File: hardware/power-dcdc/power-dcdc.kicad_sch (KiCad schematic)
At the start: 69 parts, among them J1 SOLAR_IN, J2 DCDC-MEASURES, J3 DCDC-PWM, J4 BATT2, J5 BATT1, Q1 SIR164ADP, Q2 SIR164ADP, Q3 SI7149ADP, Q4 SI7149ADP, Q5 SI7149ADP, Q6 SI7149ADP, U1 LP4951C, U2 NCP5901B, U3 PAC1953-1, U4 DGD0215, U5 DGD0215

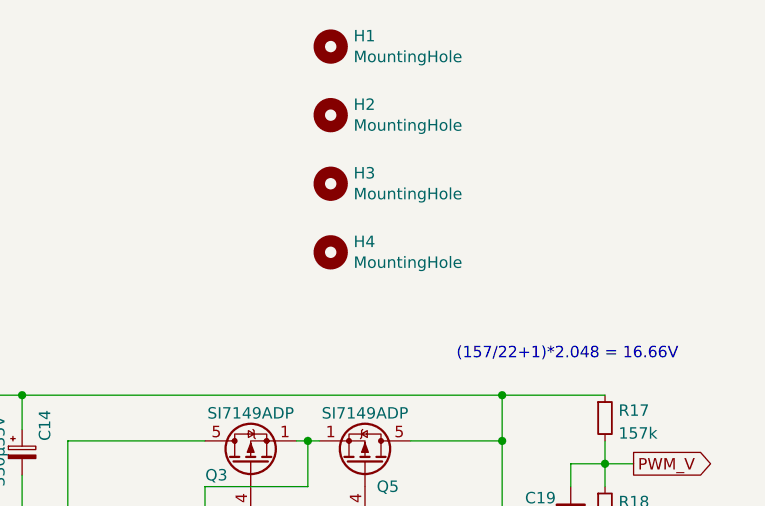
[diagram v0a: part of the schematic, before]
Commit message: Connect mounting holes to GND
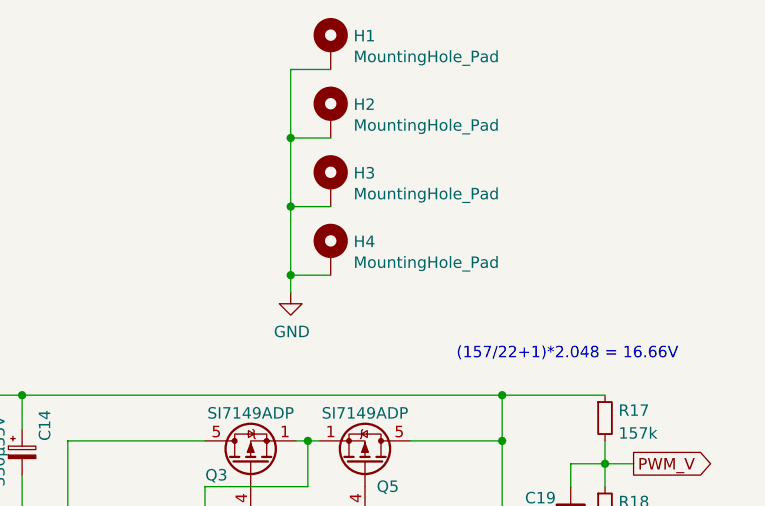
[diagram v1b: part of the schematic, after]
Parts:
- H1, H2, H3, H4: value MountingHole -> MountingHole_Pad; footprint MountingHole:MountingHole_3.2mm_M3_DIN965 -> MountingHole:MountingHole_3.2mm_M3_DIN965_Pad; symbol Mechanical:MountingHole -> Mechanical:MountingHole_Pad
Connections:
- net GND: now also H1.1, H2.1, H3.1, H4.1
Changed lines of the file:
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@@
   (junction (at 59.69 139.7) (diameter 0) (color 0 0 0 0)
   )
+  (junction (at 234.315 29.845) (diameter 0) (color 0 0 0 0)
+  )
   (junction (at 96.52 29.21) (diameter 0) (color 0 0 0 0)
   )
@@
   )
   (junction (at 114.3 73.66) (diameter 0) (color 0 0 0 0)
+  )
+  (junction (at 234.315 45.085) (diameter 0) (color 0 0 0 0)
+  )
+  (junction (at 234.315 37.465) (diameter 0) (color 0 0 0 0)
   )
   (junction (at 81.28 40.64) (diameter 0) (color 0 0 0 0)
@@
     (stroke (width 0) (type default) (color 0 0 0 0))
   )
+  (wire (pts (xy 234.315 37.465) (xy 234.315 29.845))
+    (stroke (width 0) (type default) (color 0 0 0 0))
+  )
   (wire (pts (xy 157.48 134.62) (xy 191.77 134.62))
     (stroke (width 0) (type default) (color 0 0 0 0))
@@
     (stroke (width 0) (type default) (color 0 0 0 0))
   )
+  (wire (pts (xy 234.315 37.465) (xy 238.76 37.465))
+    (stroke (width 0) (type default) (color 0 0 0 0))
+  )
   (wire (pts (xy 109.855 114.3) (xy 109.855 119.38))
     (stroke (width 0) (type default) (color 0 0 0 0))
@@
     (stroke (width 0) (type default) (color 0 0 0 0))
   )
+  (wire (pts (xy 234.315 29.845) (xy 238.76 29.845))
+    (stroke (width 0) (type default) (color 0 0 0 0))
+  )
   (wire (pts (xy 234.95 97.79) (xy 236.22 97.79))
     (stroke (width 0) (type default) (color 0 0 0 0))
@@
     (stroke (width 0) (type default) (color 0 0 0 0))
   )
+  (wire (pts (xy 234.315 45.085) (xy 238.76 45.085))
+    (stroke (width 0) (type default) (color 0 0 0 0))
+  )
   (wire (pts (xy 104.14 29.21) (xy 104.14 33.02))
     (stroke (width 0) (type default) (color 0 0 0 0))
@@
     (stroke (width 0) (type default) (color 0 0 0 0))
   )
+  (wire (pts (xy 234.315 29.845) (xy 234.315 22.225))
+    (stroke (width 0) (type default) (color 0 0 0 0))
+  )
   (wire (pts (xy 81.28 38.1) (xy 81.28 40.64))
     (stroke (width 0) (type default) (color 0 0 0 0))
@@
     (stroke (width 0) (type default) (color 0 0 0 0))
   )
+  (wire (pts (xy 234.315 46.99) (xy 234.315 45.085))
+    (stroke (width 0) (type default) (color 0 0 0 0))
+  )
   (wire (pts (xy 83.82 139.7) (xy 83.82 119.38))
     (stroke (width 0) (type default) (color 0 0 0 0))
@@
     (stroke (width 0) (type default) (color 0 0 0 0))
   )
+  (wire (pts (xy 234.315 45.085) (xy 234.315 37.465))
+    (stroke (width 0) (type default) (color 0 0 0 0))
+  )
   (wire (pts (xy 105.41 134.62) (xy 105.41 142.24))
     (stroke (width 0) (type default) (color 0 0 0 0))
@@
   )
   (wire (pts (xy 93.98 54.61) (xy 96.52 54.61))
+    (stroke (width 0) (type default) (color 0 0 0 0))
+  )
+  (wire (pts (xy 234.315 22.225) (xy 238.76 22.225))
     (stroke (width 0) (type default) (color 0 0 0 0))
   )
@@
     (pin "2")
   )
-  (symbol (lib_id "Mechanical:MountingHole") (at 238.76 19.685 0) (unit 1)
+  (symbol (lib_id "Mechanical:MountingHole_Pad") (at 238.76 19.685 0) (unit 1)
     (in_bom yes) (on_board yes)
     (property "Reference" "H1" (id 0) (at 241.3 18.5166 0)
       (effects (font (size 1.27 1.27)) (justify left))
     )
-    (property "Value" "MountingHole" (id 1) (at 241.3 20.828 0)
-      (effects (font (size 1.27 1.27)) (justify left))
-    )
-    (property "Footprint" "MountingHole:MountingHole_3.2mm_M3_DIN965" (id 2) (at 238.76 19.685 0)
+    (property "Value" "MountingHole_Pad" (id 1) (at 241.3 20.828 0)
+      (effects (font (size 1.27 1.27)) (justify left))
+    )
+    (property "Footprint" "MountingHole:MountingHole_3.2mm_M3_DIN965_Pad" (id 2) (at 238.76 19.685 0)
       (effects (font (size 1.27 1.27)) hide)
     )
@@
       (effects (font (size 1.27 1.27)) hide)
     )
+    (pin "1")
   )
   (symbol (lib_id "Device:C_Small") (at 132.08 48.26 270) (unit 1)
@@
     (pin "1")
   )
-  (symbol (lib_id "Mechanical:MountingHole") (at 238.76 42.545 0) (unit 1)
+  (symbol (lib_id "Mechanical:MountingHole_Pad") (at 238.76 42.545 0) (unit 1)
     (in_bom yes) (on_board yes)
     (property "Reference" "H4" (id 0) (at 241.3 41.3766 0)
       (effects (font (size 1.27 1.27)) (justify left))
     )
-    (property "Value" "MountingHole" (id 1) (at 241.3 43.688 0)
-      (effects (font (size 1.27 1.27)) (justify left))
-    )
-    (property "Footprint" "MountingHole:MountingHole_3.2mm_M3_DIN965" (id 2) (at 238.76 42.545 0)
+    (property "Value" "MountingHole_Pad" (id 1) (at 241.3 43.688 0)
+      (effects (font (size 1.27 1.27)) (justify left))
+    )
+    (property "Footprint" "MountingHole:MountingHole_3.2mm_M3_DIN965_Pad" (id 2) (at 238.76 42.545 0)
       (effects (font (size 1.27 1.27)) hide)
     )
@@
       (effects (font (size 1.27 1.27)) hide)
     )
+    (pin "1")
   )
   (symbol (lib_id "power:+5V") (at 52.07 46.99 0) (unit 1)
@@
     (pin "2")
   )
-  (symbol (lib_id "Mechanical:MountingHole") (at 238.76 34.925 0) (unit 1)
+  (symbol (lib_id "Mechanical:MountingHole_Pad") (at 238.76 34.925 0) (unit 1)
     (in_bom yes) (on_board yes)
     (property "Reference" "H3" (id 0) (at 241.3 33.7566 0)
       (effects (font (size 1.27 1.27)) (justify left))
     )
-    (property "Value" "MountingHole" (id 1) (at 241.3 36.068 0)
-      (effects (font (size 1.27 1.27)) (justify left))
-    )
-    (property "Footprint" "MountingHole:MountingHole_3.2mm_M3_DIN965" (id 2) (at 238.76 34.925 0)
+    (property "Value" "MountingHole_Pad" (id 1) (at 241.3 36.068 0)
+      (effects (font (size 1.27 1.27)) (justify left))
+    )
+    (property "Footprint" "MountingHole:MountingHole_3.2mm_M3_DIN965_Pad" (id 2) (at 238.76 34.925 0)
       (effects (font (size 1.27 1.27)) hide)
     )
@@
       (effects (font (size 1.27 1.27)) hide)
     )
+    (pin "1")
   )
   (symbol (lib_id "power:GND") (at 234.95 142.24 270) (unit 1)
@@
     (pin "2")
   )
-  (symbol (lib_id "Mechanical:MountingHole") (at 238.76 27.305 0) (unit 1)
+  (symbol (lib_id "Mechanical:MountingHole_Pad") (at 238.76 27.305 0) (unit 1)
     (in_bom yes) (on_board yes)
     (property "Reference" "H2" (id 0) (at 241.3 26.1366 0)
       (effects (font (size 1.27 1.27)) (justify left))
     )
-    (property "Value" "MountingHole" (id 1) (at 241.3 28.448 0)
-      (effects (font (size 1.27 1.27)) (justify left))
-    )
-    (property "Footprint" "MountingHole:MountingHole_3.2mm_M3_DIN965" (id 2) (at 238.76 27.305 0)
+    (property "Value" "MountingHole_Pad" (id 1) (at 241.3 28.448 0)
+      (effects (font (size 1.27 1.27)) (justify left))
+    )
+    (property "Footprint" "MountingHole:MountingHole_3.2mm_M3_DIN965_Pad" (id 2) (at 238.76 27.305 0)
       (effects (font (size 1.27 1.27)) hide)
     )
@@
       (effects (font (size 1.27 1.27)) hide)
     )
+    (pin "1")
   )
   (symbol (lib_id "Device:R_Small") (at 111.76 142.24 270) (unit 1)
@@
     )
     (property "Datasheet" "" (id 3) (at 86.36 90.17 0)
+      (effects (font (size 1.27 1.27)) hide)
+    )
+    (pin "1")
+  )
+  (symbol (lib_id "power:GND") (at 234.315 46.99 0) (unit 1)
+    (in_bom yes) (on_board yes)
+    (property "Reference" "#PWR024" (id 0) (at 234.315 53.34 0)
+      (effects (font (size 1.27 1.27)) hide)
+    )
+    (property "Value" "GND" (id 1) (at 234.442 51.3842 0))
+    (property "Footprint" "" (id 2) (at 234.315 46.99 0)
+      (effects (font (size 1.27 1.27)) hide)
+    )
+    (property "Datasheet" "" (id 3) (at 234.315 46.99 0)
       (effects (font (size 1.27 1.27)) hide)
     )
@@
       (reference "#PWR023") (unit 1) (value "GND") (footprint "")
     )
+    (path "/d0316b86-13cf-41da-ae94-6e550ef1990f"
+      (reference "#PWR024") (unit 1) (value "GND") (footprint "")
+    )
     (path "/e2f6369a-02b5-4d5b-ba47-235a0926e866"
       (reference "C1") (unit 1) (value "YFF31HC") (footprint "local:C_filter_1206")
@@
     )
     (path "/1e487dd6-ed86-421b-b7c0-9a9e02f46e66"
-      (reference "H1") (unit 1) (value "MountingHole") (footprint "MountingHole:MountingHole_3.2mm_M3_DIN965")
+      (reference "H1") (unit 1) (value "MountingHole_Pad") (footprint "MountingHole:MountingHole_3.2mm_M3_DIN965_Pad")
     )
     (path "/b986ae44-aeaa-4fb0-b116-e1d4a0c5aba2"
-      (reference "H2") (unit 1) (value "MountingHole") (footprint "MountingHole:MountingHole_3.2mm_M3_DIN965")
+      (reference "H2") (unit 1) (value "MountingHole_Pad") (footprint "MountingHole:MountingHole_3.2mm_M3_DIN965_Pad")
     )
     (path "/aa969c6f-5d2b-46f2-9d16-00677a06a293"
-      (reference "H3") (unit 1) (value "MountingHole") (footprint "MountingHole:MountingHole_3.2mm_M3_DIN965")
+      (reference "H3") (unit 1) (value "MountingHole_Pad") (footprint "MountingHole:MountingHole_3.2mm_M3_DIN965_Pad")
     )
     (path "/22812a7a-1ebf-4a05-8131-0142c56572c4"
-      (reference "H4") (unit 1) (value "MountingHole") (footprint "MountingHole:MountingHole_3.2mm_M3_DIN965")
+      (reference "H4") (unit 1) (value "MountingHole_Pad") (footprint "MountingHole:MountingHole_3.2mm_M3_DIN965_Pad")
     )
     (path "/aa755b7a-e588-473b-b610-150eeceb2729"

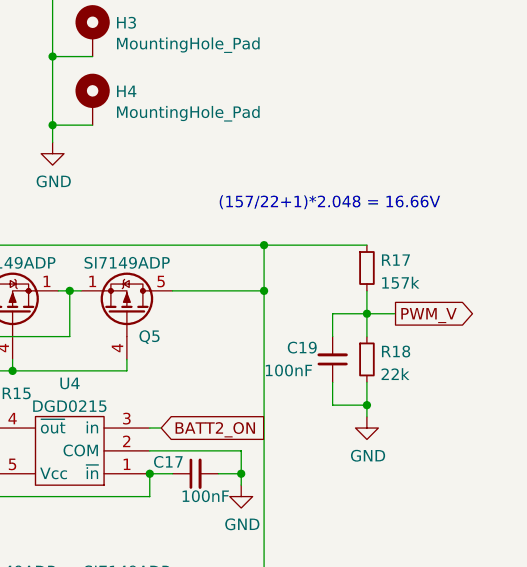
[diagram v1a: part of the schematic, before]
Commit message: Change some resistor values to match available ones.
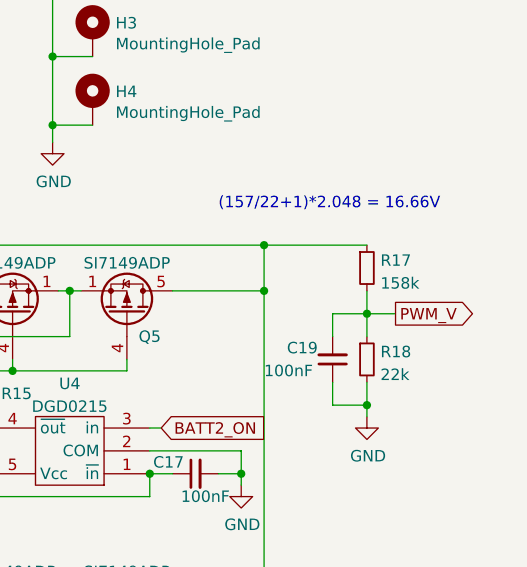
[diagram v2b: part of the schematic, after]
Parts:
- R17: value 157k -> 158k
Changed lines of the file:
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@@
       (effects (font (size 1.27 1.27)) (justify left))
     )
-    (property "Value" "157k" (id 1) (at 270.7386 62.6622 0)
+    (property "Value" "158k" (id 1) (at 270.7386 62.6622 0)
       (effects (font (size 1.27 1.27)) (justify left))
     )
@@
     )
     (path "/b417ac19-37b1-4efe-b1ee-3d38950c8e30"
-      (reference "R17") (unit 1) (value "157k") (footprint "Resistor_SMD:R_0805_2012Metric_Pad1.20x1.40mm_HandSolder")
+      (reference "R17") (unit 1) (value "158k") (footprint "Resistor_SMD:R_0805_2012Metric_Pad1.20x1.40mm_HandSolder")
     )
     (path "/b3d072d8-b65a-4fbe-9091-9d81eb179610"

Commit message: Final pass on part numbers
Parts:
- C1, C15, C16: P/N YFF31HC2A104M -> YFF31HC2A104M (M)
- C11: P/N C1206C104K5RACTU -> C1206C104K5RACTU (M)
- C13, C14, C5, C6: P/N A780MS337M1VLAS020 -> A780MS337M1VLAS020 (F)
- C3, C4: P/N GRM31CR71H475KA12L -> GRM31CR71H475KA12L (M)
- C9: P/N CL31A226KAHNNN -> CL31A226KAHNNN (M)
- D1: P/N (none) -> SMBJ28A (F)
- D2, D3: P/N (none) -> SMBJ16Ae3/TR13 (M)
- H1, H2, H3, H4: P/N (none) -> N/A
- J2, J3: P/N SSW-105-01-T-D -> SSW-105-01-T-D (F)
- L1: P/N 2305-H-RC -> 2305-H-RC (M)
- Q1, Q2: P/N SIR164ADP-T1-GE3 -> SIR164ADP-T1-GE3 (F)
- Q3, Q4, Q5, Q6: P/N SIR164ADP-T1-GE3 -> SI7149ADP-T1-GE3 (M)
- R17: P/N (none) -> CR0805-FX-1583ELF (M)
- R18, R2: P/N (none) -> WF08P2202FTL (F)
- R3: P/N (none) -> stock
- R6: P/N (none) -> WF08P2703FTL (F)
- TH1: P/N NT06104F3950B1H -> NT06104F3950B1H (M)
- U1: P/N LP4951CM/NOPB -> LP4951CM/NOPB (M)
- U2: P/N NCP5901BDR2G -> NCP5901BDR2G (M)
- U4, U5: P/N DGD0215 -> DGD0215WT-7 (M)
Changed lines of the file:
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@@
       (effects (font (size 1.27 1.27)) hide)
     )
-    (property "P/N" "DGD0215" (id 4) (at 236.22 81.28 0)
+    (property "P/N" "DGD0215WT-7 (M)" (id 4) (at 236.22 81.28 0)
       (effects (font (size 1.27 1.27)) hide)
     )
@@
       (effects (font (size 1.27 1.27)) hide)
     )
-    (property "P/N" "A780MS337M1VLAS020" (id 4) (at 204.47 64.77 0)
+    (property "P/N" "A780MS337M1VLAS020 (F)" (id 4) (at 204.47 64.77 0)
       (effects (font (size 1.27 1.27)) hide)
     )
@@
       (effects (font (size 1.27 1.27)) hide)
     )
-    (property "P/N" "A780MS337M1VLAS020" (id 4) (at 104.14 35.56 0)
+    (property "P/N" "A780MS337M1VLAS020 (F)" (id 4) (at 104.14 35.56 0)
       (effects (font (size 1.27 1.27)) hide)
     )
@@
     )
     (property "Datasheet" "https://www.vishay.com/docs/88301/15ke.pdf" (id 3) (at 245.11 148.59 0)
+      (effects (font (size 1.27 1.27)) hide)
+    )
+    (property "P/N" " SMBJ16Ae3/TR13 (M)" (id 4) (at 245.11 147.32 0)
       (effects (font (size 1.27 1.27)) hide)
     )
@@
       (effects (font (size 1.27 1.27)) hide)
     )
-    (property "P/N" "NCP5901BDR2G" (id 4) (at 132.08 59.69 0)
+    (property "P/N" "NCP5901BDR2G (M)" (id 4) (at 132.08 59.69 0)
       (effects (font (size 1.27 1.27)) hide)
     )
@@
       (effects (font (size 1.27 1.27)) hide)
     )
+    (property "P/N" "N/A" (id 4) (at 238.76 19.685 0)
+      (effects (font (size 1.27 1.27)) hide)
+    )
     (pin "1")
   )
@@
       (effects (font (size 1.27 1.27)) hide)
     )
-    (property "P/N" "SIR164ADP-T1-GE3" (id 4) (at 154.94 66.04 0)
+    (property "P/N" "SIR164ADP-T1-GE3 (F)" (id 4) (at 154.94 66.04 0)
       (effects (font (size 1.27 1.27)) hide)
     )
@@
       (effects (font (size 1.27 1.27)) hide)
     )
+    (property "P/N" "N/A" (id 4) (at 238.76 42.545 0)
+      (effects (font (size 1.27 1.27)) hide)
+    )
     (pin "1")
   )
@@
       (effects (font (size 1.27 1.27)) hide)
     )
-    (property "P/N" "SIR164ADP-T1-GE3" (id 4) (at 154.94 50.8 0)
+    (property "P/N" "SIR164ADP-T1-GE3 (F)" (id 4) (at 154.94 50.8 0)
       (effects (font (size 1.27 1.27)) hide)
     )
@@
       (effects (font (size 1.27 1.27)) hide)
     )
+    (property "P/N" "WF08P2202FTL (F)" (id 4) (at 56.515 73.025 0)
+      (effects (font (size 1.27 1.27)) hide)
+    )
     (pin "1")
     (pin "2")
@@
       (effects (font (size 1.27 1.27)) hide)
     )
-    (property "P/N" "A780MS337M1VLAS020" (id 4) (at 96.52 35.56 0)
+    (property "P/N" "A780MS337M1VLAS020 (F)" (id 4) (at 96.52 35.56 0)
       (effects (font (size 1.27 1.27)) hide)
     )
@@
       (effects (font (size 1.27 1.27)) hide)
     )
-    (property "P/N" "A780MS337M1VLAS020" (id 4) (at 196.85 64.77 0)
+    (property "P/N" "A780MS337M1VLAS020 (F)" (id 4) (at 196.85 64.77 0)
       (effects (font (size 1.27 1.27)) hide)
     )
@@
       (effects (font (size 1.27 1.27)) hide)
     )
-    (property "P/N" "YFF31HC2A104M" (id 4) (at 236.22 137.16 0)
+    (property "P/N" "YFF31HC2A104M (M)" (id 4) (at 236.22 137.16 0)
       (effects (font (size 1.27 1.27)) hide)
     )
@@
       (effects (font (size 1.27 1.27)) (justify left) hide)
     )
-    (property "P/N" "SIR164ADP-T1-GE3" (id 4) (at 229.87 66.04 0)
+    (property "P/N" " SI7149ADP-T1-GE3 (M)" (id 4) (at 229.87 66.04 0)
       (effects (font (size 1.27 1.27)) hide)
     )
@@
       (effects (font (size 1.27 1.27)) (justify left) hide)
     )
-    (property "P/N" "SIR164ADP-T1-GE3" (id 4) (at 229.87 100.33 0)
+    (property "P/N" " SI7149ADP-T1-GE3 (M)" (id 4) (at 229.87 100.33 0)
       (effects (font (size 1.27 1.27)) hide)
     )
@@
     )
     (property "Datasheet" "https://www.vishay.com/docs/88301/15ke.pdf" (id 3) (at 245.11 135.89 0)
+      (effects (font (size 1.27 1.27)) hide)
+    )
+    (property "P/N" " SMBJ16Ae3/TR13 (M)" (id 4) (at 245.11 134.62 0)
       (effects (font (size 1.27 1.27)) hide)
     )
@@
       (effects (font (size 1.27 1.27)) hide)
     )
+    (property "P/N" "WF08P2703FTL (F)" (id 4) (at 86.36 49.53 0)
+      (effects (font (size 1.27 1.27)) hide)
+    )
     (pin "1")
     (pin "2")
@@
       (effects (font (size 1.27 1.27)) hide)
     )
-    (property "P/N" " NT06104F3950B1H " (id 4) (at 142.875 89.535 0)
+    (property "P/N" "NT06104F3950B1H (M)" (id 4) (at 142.875 89.535 0)
       (effects (font (size 1.27 1.27)) hide)
     )
@@
       (effects (font (size 1.27 1.27)) hide)
     )
+    (property "P/N" "N/A" (id 4) (at 238.76 34.925 0)
+      (effects (font (size 1.27 1.27)) hide)
+    )
     (pin "1")
   )
@@
       (effects (font (size 1.27 1.27)) hide)
     )
-    (property "P/N" "GRM31CR71H475KA12L" (id 4) (at 88.9 35.56 0)
+    (property "P/N" "GRM31CR71H475KA12L (M)" (id 4) (at 88.9 35.56 0)
       (effects (font (size 1.27 1.27)) hide)
     )
@@
       (effects (font (size 1.27 1.27)) hide)
     )
+    (property "P/N" "WF08P2202FTL (F)" (id 4) (at 269.24 71.12 0)
+      (effects (font (size 1.27 1.27)) hide)
+    )
     (pin "1")
     (pin "2")
@@
     )
     (property "Datasheet" "~" (id 3) (at 269.24 60.96 0)
+      (effects (font (size 1.27 1.27)) hide)
+    )
+    (property "P/N" "CR0805-FX-1583ELF (M)" (id 4) (at 269.24 60.96 0)
       (effects (font (size 1.27 1.27)) hide)
     )
@@
       (effects (font (size 1.27 1.27)) (justify left) hide)
     )
-    (property "P/N" "SIR164ADP-T1-GE3" (id 4) (at 242.57 100.33 0)
+    (property "P/N" " SI7149ADP-T1-GE3 (M)" (id 4) (at 242.57 100.33 0)
       (effects (font (size 1.27 1.27)) hide)
     )
@@
       (effects (font (size 1.27 1.27)) hide)
     )
+    (property "P/N" " SMBJ28A (F)" (id 4) (at 59.69 146.05 0)
+      (effects (font (size 1.27 1.27)) hide)
+    )
     (pin "1")
     (pin "2")
@@
     )
     (property "Datasheet" "~" (id 3) (at 238.76 27.305 0)
+      (effects (font (size 1.27 1.27)) hide)
+    )
+    (property "P/N" "N/A" (id 4) (at 238.76 27.305 0)
       (effects (font (size 1.27 1.27)) hide)
     )
@@
       (effects (font (size 1.27 1.27)) hide)
     )
-    (property "P/N" "C1206C104K5RACTU" (id 4) (at 181.61 64.77 0)
+    (property "P/N" "C1206C104K5RACTU (M)" (id 4) (at 181.61 64.77 0)
       (effects (font (size 1.27 1.27)) hide)
     )
@@
     )
     (property "Datasheet" "~" (id 3) (at 56.515 84.455 0)
+      (effects (font (size 1.27 1.27)) hide)
+    )
+    (property "P/N" "stock" (id 4) (at 56.515 84.455 0)
       (effects (font (size 1.27 1.27)) hide)
     )
@@
       (effects (font (size 1.27 1.27)) (justify left) hide)
     )
-    (property "P/N" "SIR164ADP-T1-GE3" (id 4) (at 242.57 66.04 0)
+    (property "P/N" " SI7149ADP-T1-GE3 (M)" (id 4) (at 242.57 66.04 0)
       (effects (font (size 1.27 1.27)) hide)
     )
@@
       (effects (font (size 1.27 1.27)) hide)
     )
-    (property "P/N" " SSW-105-01-T-D " (id 4) (at 93.345 90.17 0)
+    (property "P/N" " SSW-105-01-T-D (F)" (id 4) (at 93.345 90.17 0)
       (effects (font (size 1.27 1.27)) hide)
     )
@@
       (effects (font (size 1.27 1.27)) hide)
     )
-    (property "P/N" "YFF31HC2A104M" (id 4) (at 236.22 149.86 0)
+    (property "P/N" "YFF31HC2A104M (M)" (id 4) (at 236.22 149.86 0)
       (effects (font (size 1.27 1.27)) hide)
     )
@@
       (effects (font (size 1.27 1.27)) hide)
     )
-    (property "P/N" "YFF31HC2A104M" (id 4) (at 66.04 147.32 0)
+    (property "P/N" "YFF31HC2A104M (M)" (id 4) (at 66.04 147.32 0)
       (effects (font (size 1.27 1.27)) hide)
     )
@@
       (effects (font (size 1.27 1.27)) hide)
     )
-    (property "P/N" " LP4951CM/NOPB " (id 4) (at 80.01 58.42 0)
+    (property "P/N" "LP4951CM/NOPB (M)" (id 4) (at 80.01 58.42 0)
       (effects (font (size 1.27 1.27)) hide)
     )
@@
       (effects (font (size 1.27 1.27)) hide)
     )
-    (property "P/N" "2305-H-RC" (id 4) (at 172.72 58.42 0)
+    (property "P/N" "2305-H-RC (M)" (id 4) (at 172.72 58.42 0)
       (effects (font (size 1.27 1.27)) hide)
     )
@@
       (effects (font (size 1.27 1.27)) hide)
     )
-    (property "P/N" "DGD0215" (id 4) (at 236.22 115.57 0)
+    (property "P/N" "DGD0215WT-7 (M)" (id 4) (at 236.22 115.57 0)
       (effects (font (size 1.27 1.27)) hide)
     )
@@
       (effects (font (size 1.27 1.27)) hide)
     )
-    (property "P/N" "CL31A226KAHNNN" (id 4) (at 119.38 68.58 0)
+    (property "P/N" "CL31A226KAHNNN (M)" (id 4) (at 119.38 68.58 0)
       (effects (font (size 1.27 1.27)) hide)
     )
@@
       (effects (font (size 1.27 1.27)) hide)
     )
-    (property "P/N" "GRM31CR71H475KA12L" (id 4) (at 81.28 35.56 0)
+    (property "P/N" "GRM31CR71H475KA12L (M)" (id 4) (at 81.28 35.56 0)
       (effects (font (size 1.27 1.27)) hide)
     )
@@
       (effects (font (size 1.27 1.27)) hide)
     )
-    (property "P/N" " SSW-105-01-T-D" (id 4) (at 92.075 116.84 0)
-      (effects (font (size 1.27 1.27)) hide)
-    )
+    (property "P/N" " SSW-105-01-T-D (F)" (id 4) (at 92.075 116.84 0)
+      (effects (font (size 1.27 1.27)) hide)
+    )
